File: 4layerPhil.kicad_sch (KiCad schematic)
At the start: 58 parts, among them J1 USB_C_Receptacle_USB2.0_16P, J2 Conn_01x05_Pin, J3 Conn_01x04_Pin, J6 1140084168, SW1 SW_SPDT, SW2 BTN1, SW3 BTN2, SW4 BTN3, U2 USBLC6-2SC6, U3 STM32F103RCTx, U4 SPX3819M5-L-3-3, Y1 16MHz

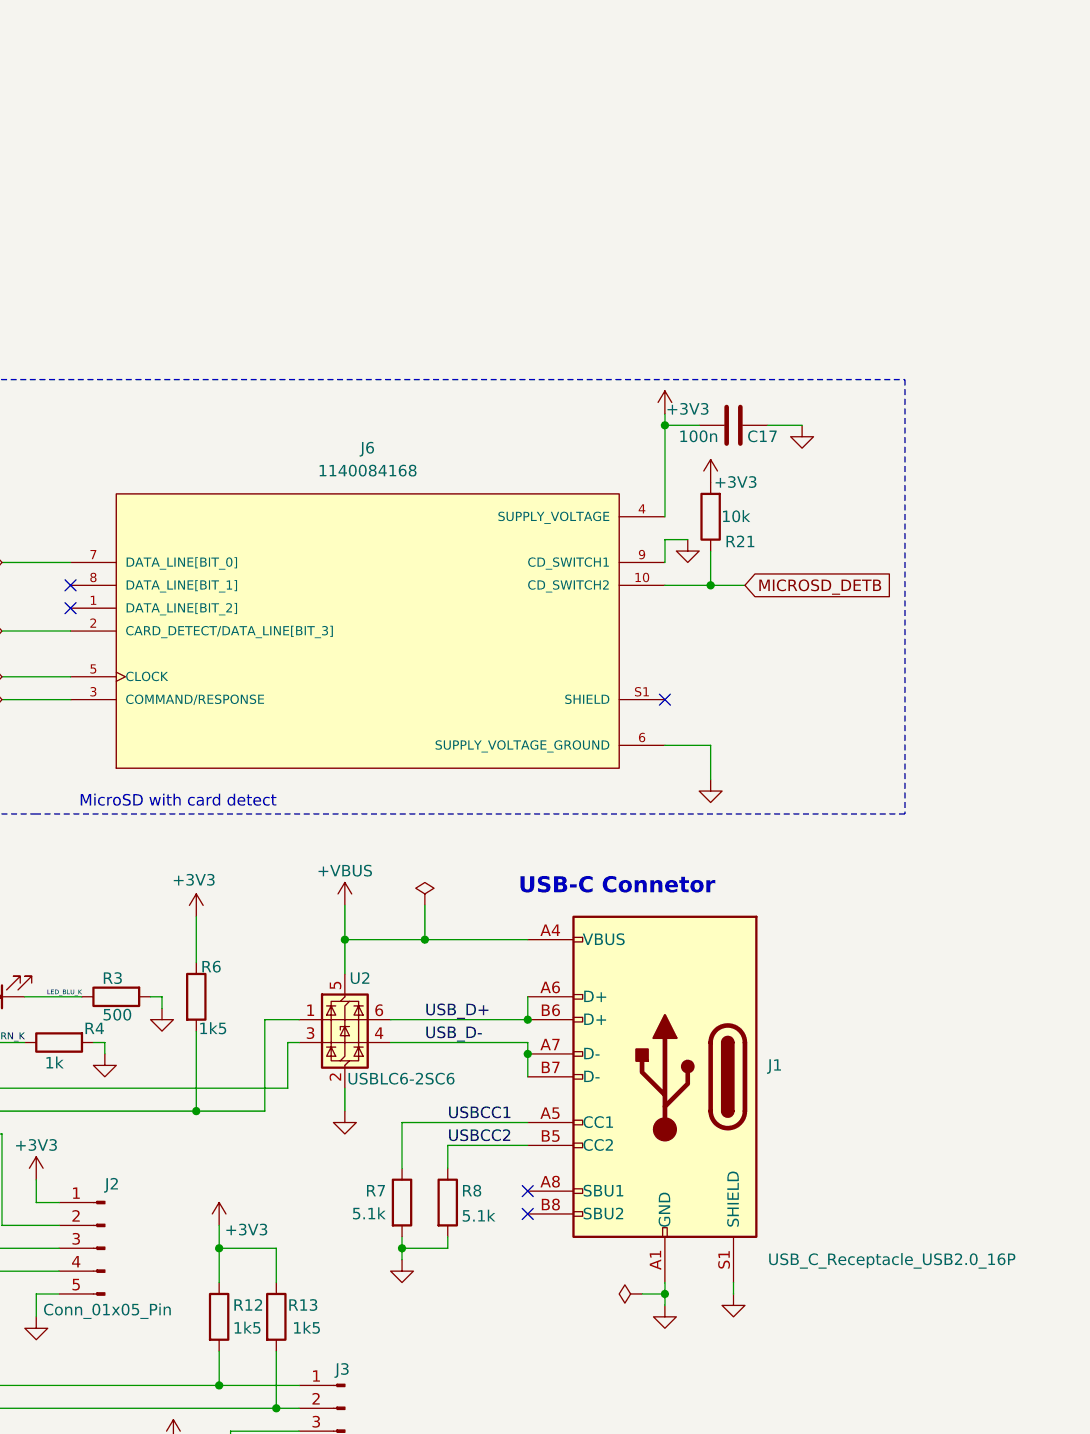
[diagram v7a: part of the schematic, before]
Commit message: New microSD card
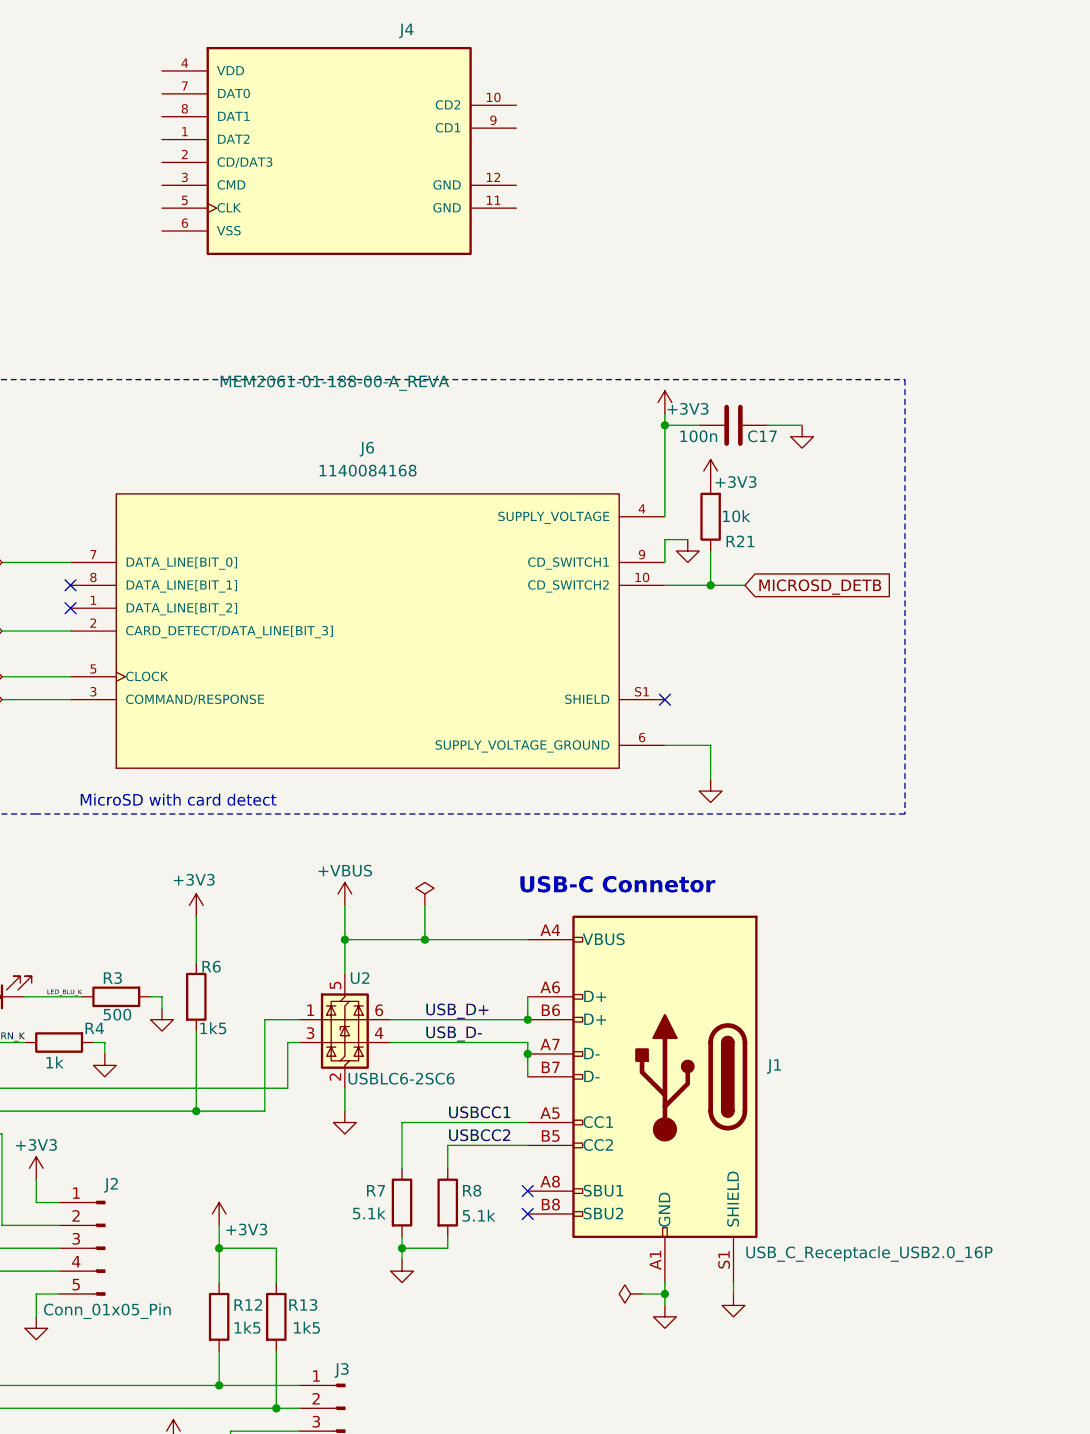
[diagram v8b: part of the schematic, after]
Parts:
- added J4: MEM2061-01-188-00-A_REVA, MEM2061-01-188-00-A_REVA:GCT_MEM2061-01-188-00-A_REVA, symbol MicroSD_Socket:MEM2061-01-188-00-A_REVA
- J6: footprint MicroSD_Socket:AMPHENOL_1140084168 -> MicroSD_Socket:GCT_MEM2061-01-188-00-A_REVA
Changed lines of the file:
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@@
 	)
 	(symbol
+		(lib_id "MicroSD_Socket:MEM2061-01-188-00-A_REVA")
+		(at 207.01 -8.89 0)
+		(unit 1)
+		(exclude_from_sim no)
+		(in_bom yes)
+		(on_board yes)
+		(dnp no)
+		(fields_autoplaced yes)
+		(property "Reference" "J4"
+			(at 228.346 -26.162 0)
+			(effects
+				(font
+					(size 1.27 1.27)
+				)
+				(justify left)
+			)
+		)
+		(property "Value" "MEM2061-01-188-00-A_REVA"
+			(at 208.28 12.954 0)
+			(effects
+				(font
+					(size 1.27 1.27)
+				)
+				(justify left)
+			)
+		)
+		(property "Footprint" "MEM2061-01-188-00-A_REVA:GCT_MEM2061-01-188-00-A_REVA"
+			(at 211.836 -45.72 0)
+			(effects
+				(font
+					(size 1.27 1.27)
+				)
+				(justify bottom)
+				(hide yes)
+			)
+		)
+		(property "Datasheet" ""
+			(at 207.01 -8.89 0)
+			(effects
+				(font
+					(size 1.27 1.27)
+				)
+				(hide yes)
+			)
+		)
+		(property "Description" ""
+			(at 207.01 -8.89 0)
+			(effects
+				(font
+					(size 1.27 1.27)
+				)
+				(hide yes)
+			)
+		)
+		(property "MF" "Global Connector Technology"
+			(at 204.216 -47.752 0)
+			(effects
+				(font
+					(size 1.27 1.27)
+				)
+				(justify bottom)
+				(hide yes)
+			)
+		)
+		(property "Description_1" "10 (8 + 2) Position Card Connector Secure Digital - microSD™ Surface Mount, Right Angle Gold"
+			(at 201.422 -40.386 0)
+			(effects
+				(font
+					(size 1.27 1.27)
+				)
+				(justify bottom)
+				(hide yes)
+			)
+		)
+		(property "Package" "None"
+			(at 203.454 -42.672 0)
+			(effects
+				(font
+					(size 1.27 1.27)
+				)
+				(justify bottom)
+				(hide yes)
+			)
+		)
+		(property "Price" "None"
+			(at 204.724 -45.466 0)
+			(effects
+				(font
+					(size 1.27 1.27)
+				)
+				(justify bottom)
+				(hide yes)
+			)
+		)
+		(property "Check_prices" "https://www.snapeda.com/parts/MEM2061-01-188-00-A/Global+Connector+Technology/view-part/?ref=eda"
+			(at 209.804 -43.18 0)
+			(effects
+				(font
+					(size 1.27 1.27)
+				)
+				(justify bottom)
+				(hide yes)
+			)
+		)
+		(property "SnapEDA_Link" "https://www.snapeda.com/parts/MEM2061-01-188-00-A/Global+Connector+Technology/view-part/?ref=snap"
+			(at 207.772 -46.99 0)
+			(effects
+				(font
+					(size 1.27 1.27)
+				)
+				(justify bottom)
+				(hide yes)
+			)
+		)
+		(property "MP" "MEM2061-01-188-00-A"
+			(at 202.946 -41.656 0)
+			(effects
+				(font
+					(size 1.27 1.27)
+				)
+				(justify bottom)
+				(hide yes)
+			)
+		)
+		(property "Purchase-URL" "https://www.snapeda.com/api/url_track_click_mouser/?unipart_id=779219&manufacturer=Global Connector Technology&part_name=MEM2061-01-188-00-A&search_term=None"
+			(at 211.074 -45.974 0)
+			(effects
+				(font
+					(size 1.27 1.27)
+				)
+				(justify bottom)
+				(hide yes)
+			)
+		)
+		(property "Availability" "In Stock"
+			(at 204.47 -35.56 0)
+			(effects
+				(font
+					(size 1.27 1.27)
+				)
+				(justify bottom)
+				(hide yes)
+			)
+		)
+		(property "MANUFACTURER" "GCT"
+			(at 206.248 -38.862 0)
+			(effects
+				(font
+					(size 1.27 1.27)
+				)
+				(justify bottom)
+				(hide yes)
+			)
+		)
+		(pin "2"
+		)
+		(pin "3"
+		)
+		(pin "8"
+		)
+		(pin "7"
+		)
+		(pin "4"
+		)
+		(pin "1"
+		)
+		(pin "6"
+		)
+		(pin "5"
+		)
+		(pin "9"
+		)
+		(pin "10"
+		)
+		(pin "11"
+		)
+		(pin "12"
+		)
+		(instances
+			(project ""
+				(path "/7ec3a92f-71da-4a6b-be29-ed63fa8d0fd2"
+					(reference "J4")
+					(unit 1)
+				)
+			)
+		)
+	)
+	(symbol
 		(lib_id "power:VBUS")
 		(at 222.25 71.12 0)
@@
 			)
 		)
-		(property "Footprint" "MicroSD_Socket:AMPHENOL_1140084168"
+		(property "Footprint" "MicroSD_Socket:GCT_MEM2061-01-188-00-A_REVA"
 			(at 224.79 40.64 0)
 			(effects
@@
 		)
 		(property "Value" "USB_C_Receptacle_USB2.0_16P"
-			(at 269.24 110.49 0)
+			(at 266.7 109.728 0)
 			(effects
 				(font
